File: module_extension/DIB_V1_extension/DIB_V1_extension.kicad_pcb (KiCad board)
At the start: 2 copper layers, 76 x 51 mm, 10 parts, among them J1 20-pin power socket, J2 28-pin module socket, J3 PROBE, J4 CABLE

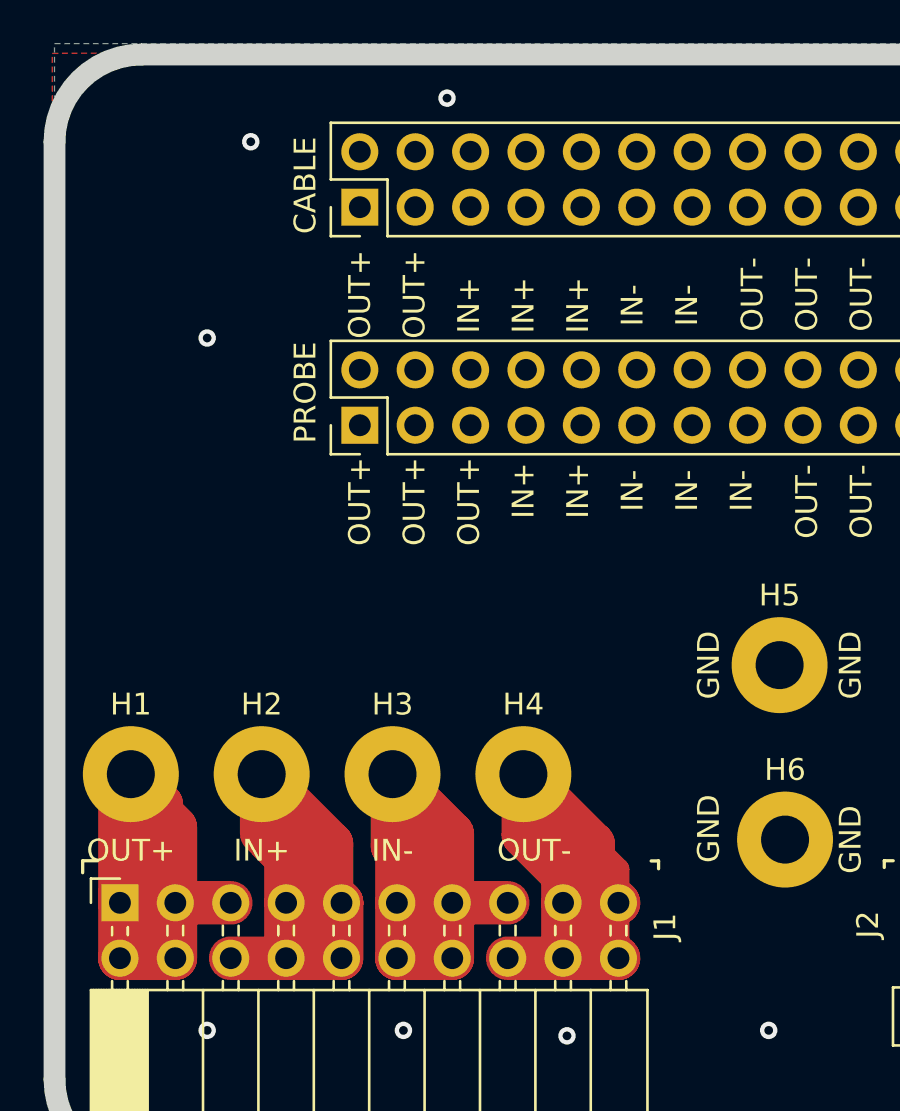
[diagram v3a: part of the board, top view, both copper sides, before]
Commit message: Changing pinout fix #3 fix #1
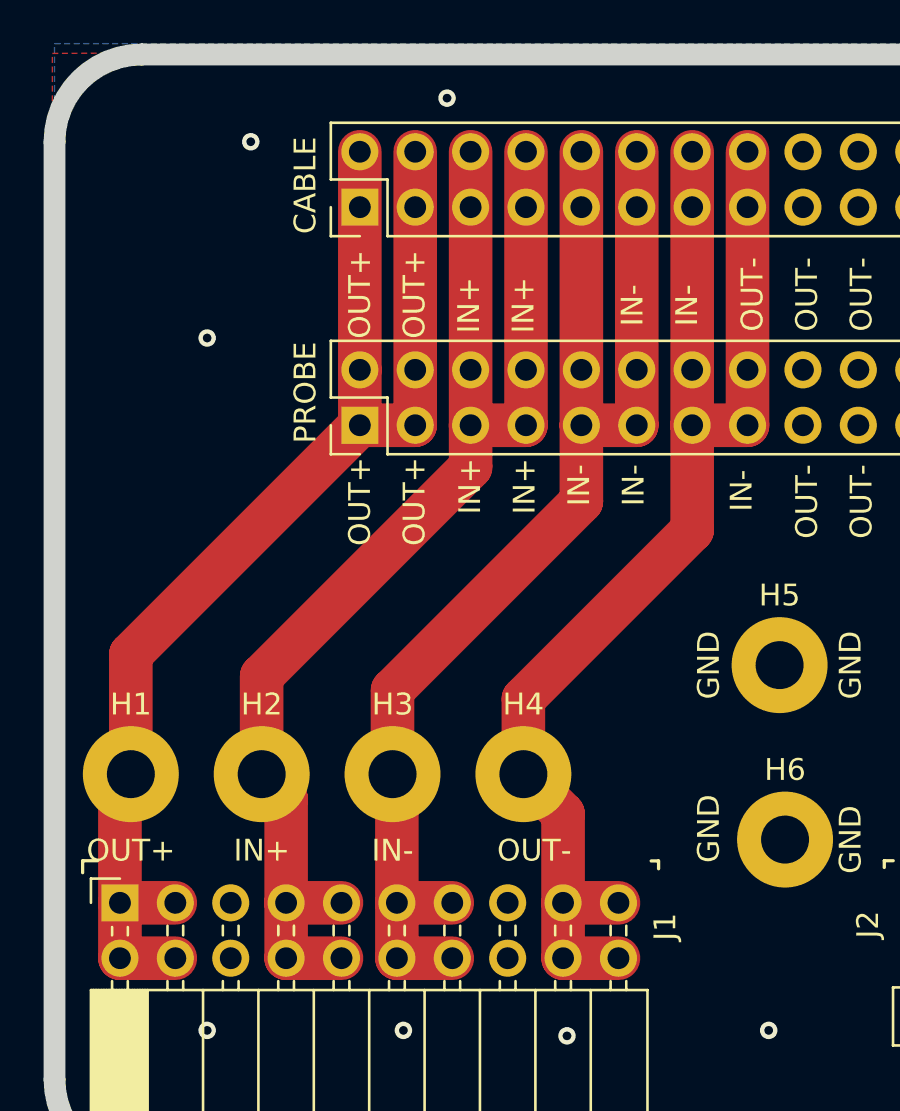
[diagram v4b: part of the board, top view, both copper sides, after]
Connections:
- J1 pad 15: IN- -> OUT-
- J1 pad 16: OUT- -> IN-
- J1 pad 5: OUT+ -> IN+
- J1 pad 6: IN+ -> OUT+
- J3 pad 36: DIB_BOOT -> +12V
- J3 pad 37: UART_TX -> 5V
- J3 pad 38: UART_RX -> DIB_BOOT
- J3 pad 39: 5V -> UART_TX
- J3 pad 40: +12V -> UART_RX
- J4 pad 36: DIB_BOOT -> +12V
- J4 pad 37: UART_TX -> 5V
- J4 pad 38: UART_RX -> DIB_BOOT
- J4 pad 39: 5V -> UART_TX
- J4 pad 40: +12V -> UART_RX
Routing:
- net OUT+: track 32.5 -> 61.7 mm
- net IN+: track 33.5 -> 61.6 mm
- net IN-: track 33.1 -> 60.8 mm
- net OUT-: track 33.8 -> 61.1 mm

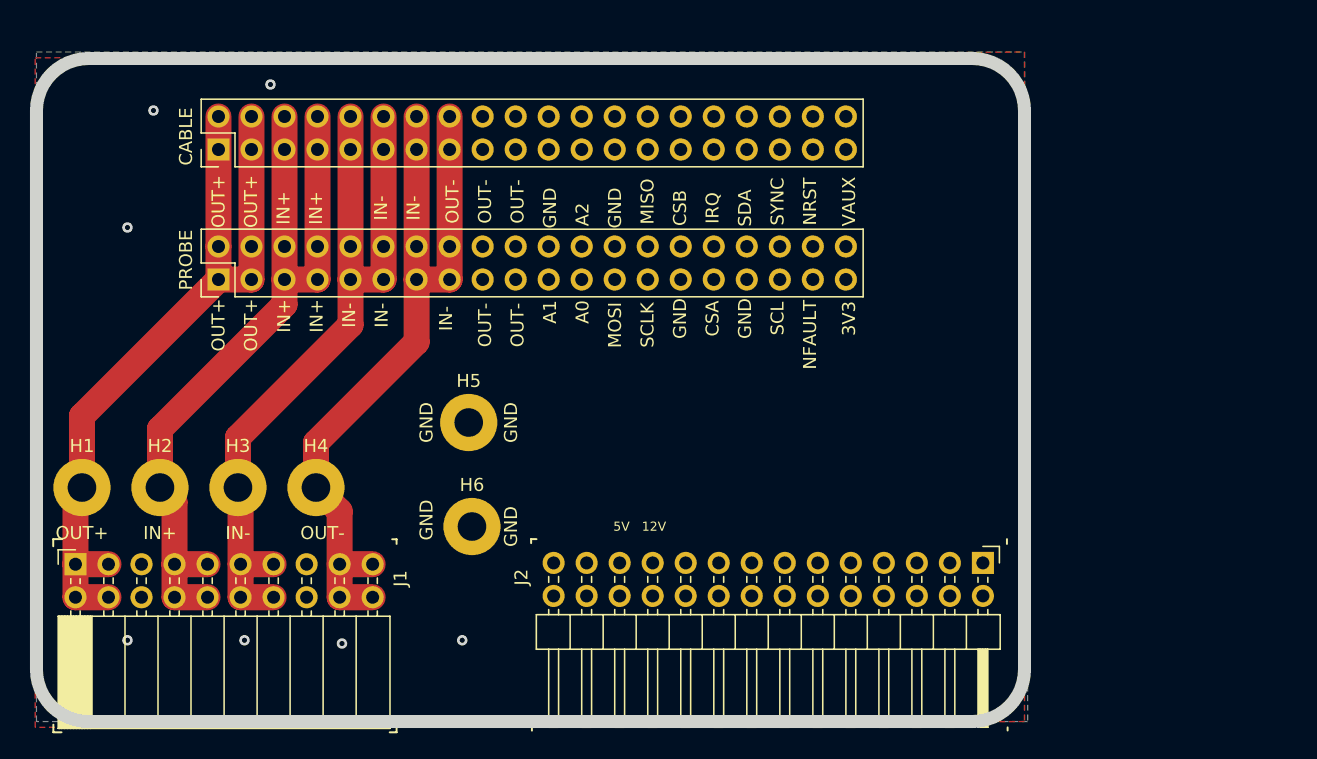
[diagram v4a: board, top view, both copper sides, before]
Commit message: Routing, adding mounting holesFix #2
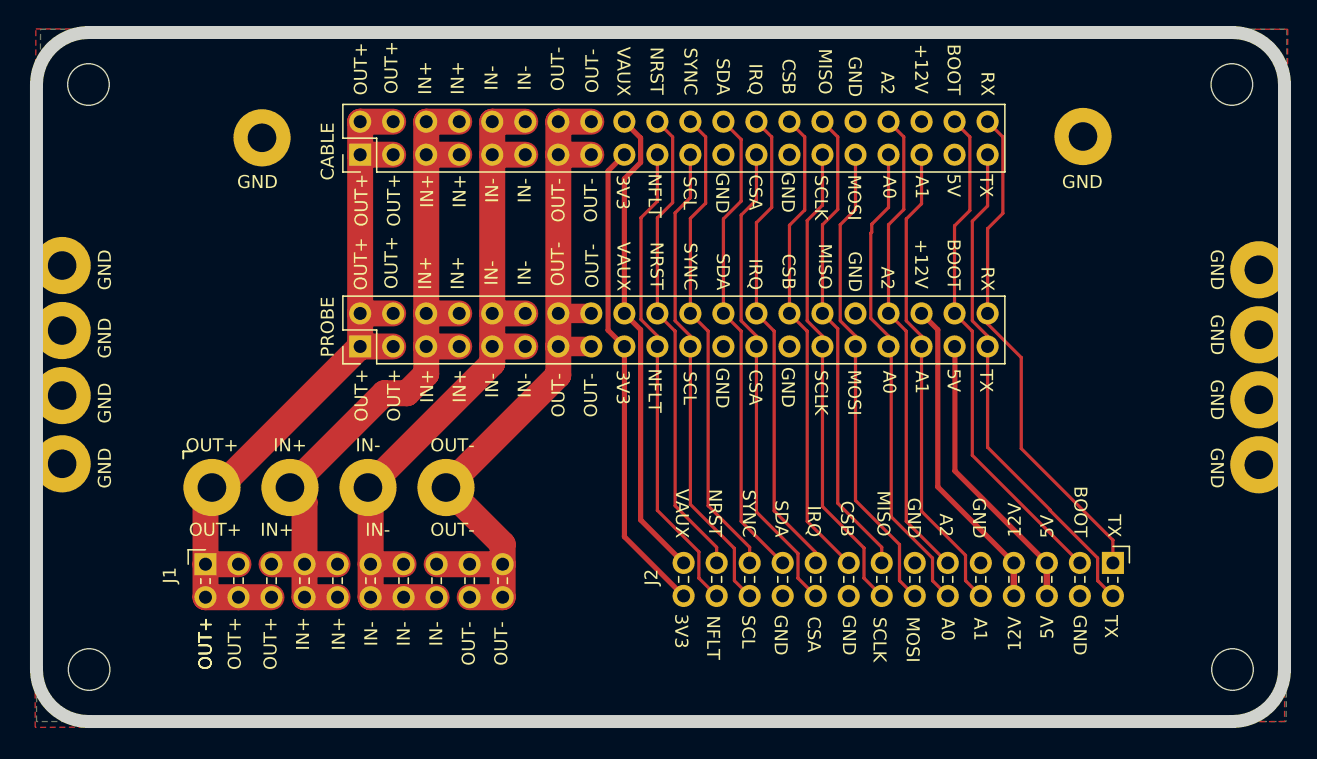
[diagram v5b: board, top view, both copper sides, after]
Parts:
- added H10: MH, MountingHole:MountingHole_3.2mm_M3, F.Cu at (165.3, 131.6)
- added H5: GND, MountingHole:MountingHole_2.2mm_M2_Pad, F.Cu at (75.3, 100.5)
- added H5: GND, MountingHole:MountingHole_2.2mm_M2_Pad, F.Cu at (75.3, 105.5)
- added H5: GND, MountingHole:MountingHole_2.2mm_M2_Pad, F.Cu at (75.3, 110.5)
- added H5: GND, MountingHole:MountingHole_2.2mm_M2_Pad, F.Cu at (75.3, 115.8)
- added H5: GND, MountingHole:MountingHole_2.2mm_M2_Pad, F.Cu at (167.3, 115.8)
- added H5: GND, MountingHole:MountingHole_2.2mm_M2_Pad, F.Cu at (167.3, 110.8)
- added H5: GND, MountingHole:MountingHole_2.2mm_M2_Pad, F.Cu at (167.3, 105.8)
- added H5: GND, MountingHole:MountingHole_2.2mm_M2_Pad, F.Cu at (167.3, 100.8)
- added H7: MH, MountingHole:MountingHole_3.2mm_M3, F.Cu at (77.3, 86.6)
- added H8: MH, MountingHole:MountingHole_3.2mm_M3, F.Cu at (77.3, 131.6)
- added H9: MH, MountingHole:MountingHole_3.2mm_M3, F.Cu at (165.2, 86.6)
- moved H5 52.1 mm to (153.8, 90.6)
- moved H6 34.0 mm to (90.7, 90.7)
- moved J3 12.1 mm to (98.2, 106.8)
- moved J4 10.9 mm to (98.2, 92.0)
- moved H1 10.0 mm to (86.8, 117.6)
- moved H2 10.0 mm to (92.8, 117.6)
- moved H3 10.0 mm to (98.8, 117.6)
- moved H4 10.0 mm to (104.8, 117.6)
- moved J1 10.0 mm to (86.3, 123.5)
- moved J2 10.0 mm to (156.1, 123.4)
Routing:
- net DIB_BOOT: track 0.00 -> 38.9 mm
- net UART_TX: track 0.00 -> 38.9 mm
- net UART_RX: track 0.00 -> 38.9 mm
- net DIB_A0: track 0.00 -> 37.0 mm
- net DIB_SDA: track 0.00 -> 37.0 mm
- net DIB_NFAULT: track 0.00 -> 36.9 mm
- net DIB_+3V3: track 0.00 -> 36.9 mm
- net +VAUX: track 0.00 -> 36.9 mm
- net DIB_MISO: track 0.00 -> 36.8 mm
- net DIB_SYNC: track 0.00 -> 36.8 mm
- net DIB_CSB: track 0.00 -> 36.8 mm
- net DIB_CSA: track 0.00 -> 36.8 mm
- net DIB_A2: track 0.00 -> 36.8 mm
- net DIB_A1: track 0.00 -> 36.8 mm
- net DIB_MOSI: track 0.00 -> 36.8 mm
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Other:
- board size 76 x 51 mm -> 96 x 53 mm
- rule pad_to_mask_clearance: 0.051 -> 0
- board text added: "+12V"
- board text added: "BOOT"
- board text added: "NFLT"
- board text added: "RX"
- board text added: "TX"
- board text removed: "NFAULT"

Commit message: Adding new production files
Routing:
- net 5V: track 22.1 -> 37.9 mm
- net +12V: track 24.7 -> 40.5 mm
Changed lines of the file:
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@@
     (thickness 1.6)
     (drawings 297)
-    (tracks 218)
+    (tracks 229)
     (zones 0)
     (modules 22)
@@
   (segment (start 143.95 106.78) (end 143.92 106.75) (width 0.4) (layer F.Cu) (net 1))
   (segment (start 143.95 116.33) (end 143.95 106.78) (width 0.4) (layer F.Cu) (net 1))
+  (segment (start 143.92 106.060002) (end 142.669999 104.810001) (width 0.4) (layer F.Cu) (net 1))
+  (segment (start 143.92 106.75) (end 143.92 106.060002) (width 0.4) (layer F.Cu) (net 1))
+  (segment (start 142.669999 104.810001) (end 142.669999 103.005001) (width 0.4) (layer F.Cu) (net 1))
+  (segment (start 143.92 101.755) (end 143.92 92) (width 0.4) (layer F.Cu) (net 1))
+  (segment (start 142.669999 103.005001) (end 143.92 101.755) (width 0.4) (layer F.Cu) (net 1))
   (segment (start 88.84 126.04) (end 86.3 126.04) (width 2) (layer F.Cu) (net 2))
   (segment (start 88.84 123.5) (end 86.3 123.5) (width 2) (layer F.Cu) (net 2))
@@
   (segment (start 113.44 106.75) (end 115.98 106.75) (width 1.5) (layer F.Cu) (net 5))
   (segment (start 148.48 125.94) (end 148.48 123.4) (width 0.5) (layer F.Cu) (net 6))
-  (segment (start 142.630001 105.460001) (end 141.38 104.21) (width 0.4) (layer F.Cu) (net 6))
-  (segment (start 142.630001 117.550001) (end 142.630001 105.460001) (width 0.4) (layer F.Cu) (net 6))
+  (segment (start 141.38 104.368544) (end 141.38 104.21) (width 0.4) (layer F.Cu) (net 6))
+  (segment (start 142.630001 117.550001) (end 142.630001 105.618545) (width 0.4) (layer F.Cu) (net 6))
+  (segment (start 142.630001 90.710001) (end 141.38 89.46) (width 0.4) (layer F.Cu) (net 6))
+  (segment (start 142.630001 105.618545) (end 141.38 104.368544) (width 0.4) (layer F.Cu) (net 6))
+  (segment (start 141.38 103.007919) (end 142.630001 101.757918) (width 0.4) (layer F.Cu) (net 6))
+  (segment (start 142.630001 101.757918) (end 142.630001 90.710001) (width 0.4) (layer F.Cu) (net 6))
   (segment (start 148.48 123.4) (end 142.630001 117.550001) (width 0.4) (layer F.Cu) (net 6))
+  (segment (start 141.38 104.21) (end 141.38 103.007919) (width 0.4) (layer F.Cu) (net 6))
   (segment (start 123.08 125.94) (end 118.525 121.385) (width 0.4) (layer F.Cu) (net 8))
   (segment (start 118.525 106.755) (end 118.52 106.75) (width 0.4) (layer F.Cu) (net 8))
@@
   (segment (start 145.284999 115.124999) (end 145.284999 105.574999) (width 0.25) (layer F.Cu) (net 24))
   (segment (start 153.56 123.4) (end 145.284999 115.124999) (width 0.25) (layer F.Cu) (net 24))
-  (segment (start 143.92 104.21) (end 143.92 97.47) (width 0.25) (layer F.Cu) (net 24))
+  (segment (start 145.095001 96.294999) (end 145.095001 90.635001) (width 0.25) (layer F.Cu) (net 24))
   (segment (start 145.095001 90.635001) (end 143.92 89.46) (width 0.25) (layer F.Cu) (net 24))
-  (segment (start 145.095001 96.294999) (end 145.095001 90.635001) (width 0.25) (layer F.Cu) (net 24))
-  (segment (start 143.92 97.47) (end 145.095001 96.294999) (width 0.25) (layer F.Cu) (net 24))
+  (segment (start 144.769999 103.360001) (end 144.769999 96.620001) (width 0.25) (layer F.Cu) (net 24))
+  (segment (start 144.769999 96.620001) (end 145.095001 96.294999) (width 0.25) (layer F.Cu) (net 24))
+  (segment (start 143.92 104.21) (end 144.769999 103.360001) (width 0.25) (layer F.Cu) (net 24))
   (segment (start 154.924999 123.025997) (end 151.249002 119.35) (width 0.25) (layer F.Cu) (net 25))
   (segment (start 156.1 125.94) (end 154.924999 124.764999) (width 0.25) (layer F.Cu) (net 25))
